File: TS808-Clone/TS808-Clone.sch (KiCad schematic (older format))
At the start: 44 parts, among them J1 AudioJack2, J2 Barrel_Jack, J3 AudioJack2, Q1 2N4401-AP, Q2 2N4401-AP, U1 RC4558

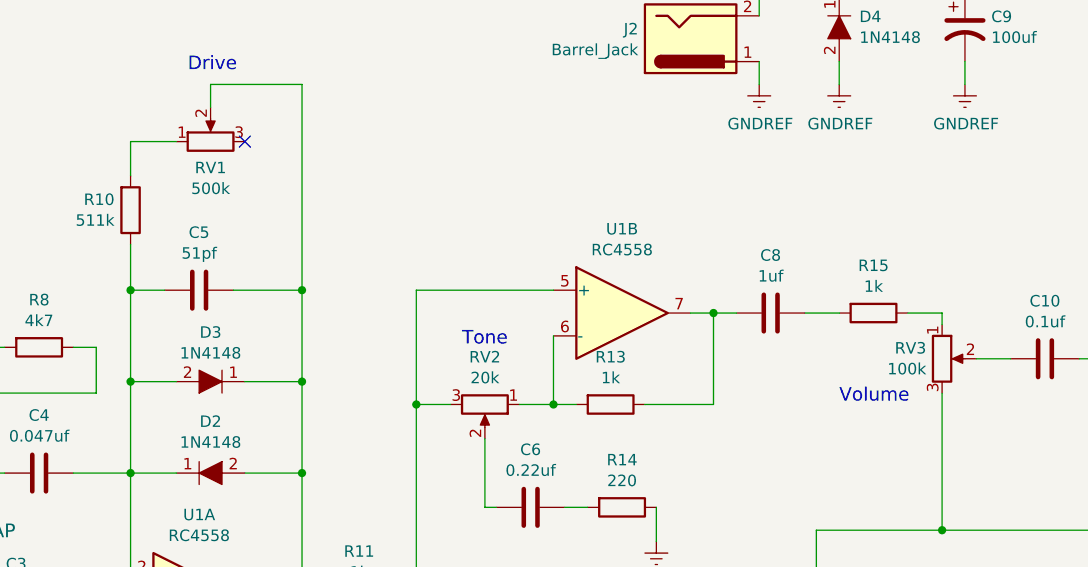
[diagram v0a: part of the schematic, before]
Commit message: Finished traces. Added fill with ground layer.
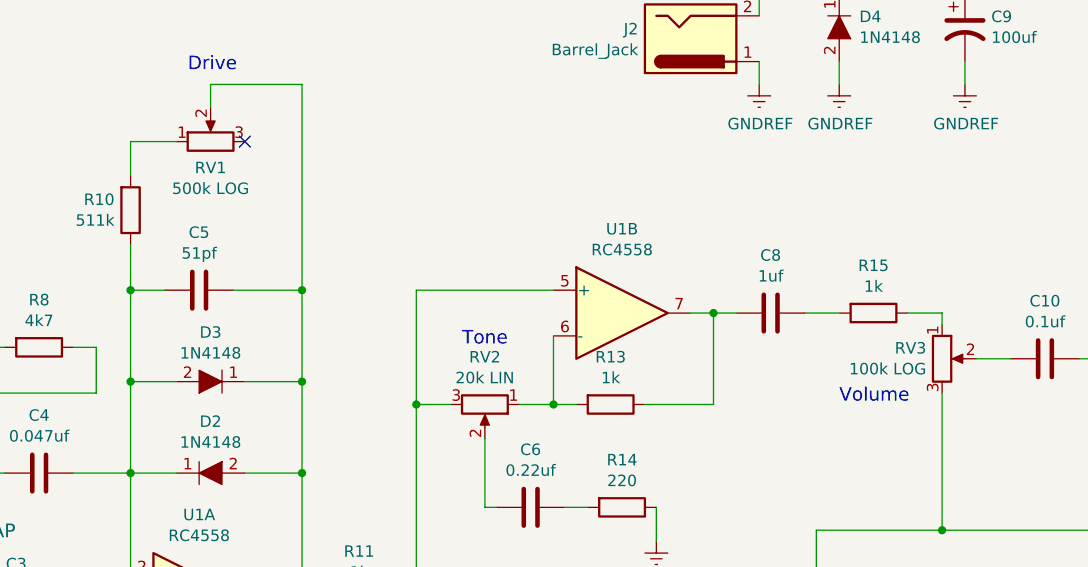
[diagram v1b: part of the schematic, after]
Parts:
- RV1: value 500k -> 500k LOG
- RV2: value 20k -> 20k LIN
- RV3: value 100k -> 100k LOG
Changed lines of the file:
@@
 P 5450 1900
 F 0 "RV1" V 5335 1900 50  0000 C CNN
-F 1 "500k" V 5244 1900 50  0000 C CNN
+F 1 "500k LOG" V 5244 1900 50  0000 C CNN
 F 2 "Potentiometer_THT:Potentiometer_TT_P0915N" H 5450 1900 50  0001 C CNN
 F 3 "https://www.ttelectronics.com/TTElectronics/media/ProductFiles/Potentiometers/Datasheets/P09x.pdf" H 5450 1900 50  0001 C CNN
@@
 P 6650 3050
 F 0 "RV2" V 6443 3050 50  0000 C CNN
-F 1 "20k" V 6534 3050 50  0000 C CNN
+F 1 "20k LIN" V 6534 3050 50  0000 C CNN
 F 2 "Potentiometer_THT:Potentiometer_TT_P0915N" H 6650 3050 50  0001 C CNN
 F 3 "https://www.ttelectronics.com/TTElectronics/media/ProductFiles/Potentiometers/Datasheets/P09x.pdf" H 6650 3050 50  0001 C CNN
@@
 P 8650 2850
 F 0 "RV3" H 8581 2896 50  0000 R CNN
-F 1 "100k" H 8581 2805 50  0000 R CNN
+F 1 "100k LOG" H 8581 2805 50  0000 R CNN
 F 2 "Potentiometer_THT:Potentiometer_TT_P0915N" H 8650 2850 50  0001 C CNN
 F 3 "https://www.ttelectronics.com/TTElectronics/media/ProductFiles/Potentiometers/Datasheets/P09x.pdf" H 8650 2850 50  0001 C CNN

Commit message: changed footprint for the pots
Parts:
- D2, D3, D4: symbol dk_Diodes-Rectifiers-Single:1N4148 -> TS808-Clone-rescue:1N4148-dk_Diodes-Rectifiers-Single
- Q1, Q2: symbol dk_Transistors-Bipolar-BJT-Single:2N4401-AP -> TS808-Clone-rescue:2N4401-AP-dk_Transistors-Bipolar-BJT-Single
- RV1, RV2, RV3: footprint Potentiometer_THT:Potentiometer_TT_P0915N -> Potentiometer_THT:Potentiometer_Bourns_PTV09A-1_Single_Vertical
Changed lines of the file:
@@
 $EndComp
 $Comp
-L dk_Diodes-Rectifiers-Single:1N4148 D4
+L TS808-Clone-rescue:1N4148-dk_Diodes-Rectifiers-Single D4
 U 1 1 5D46A900
 P 8200 1350
@@
 $EndComp
 $Comp
-L dk_Diodes-Rectifiers-Single:1N4148 D3
+L TS808-Clone-rescue:1N4148-dk_Diodes-Rectifiers-Single D3
 U 1 1 5D46D50E
 P 5500 2950
@@
 $EndComp
 $Comp
-L dk_Diodes-Rectifiers-Single:1N4148 D2
+L TS808-Clone-rescue:1N4148-dk_Diodes-Rectifiers-Single D2
 U 1 1 5D470632
 P 5400 3350
@@
 $EndComp
 $Comp
-L dk_Transistors-Bipolar-BJT-Single:2N4401-AP Q2
+L TS808-Clone-rescue:2N4401-AP-dk_Transistors-Bipolar-BJT-Single Q2
 U 1 1 5D472C75
 P 9900 2850
@@
 	2950 2500 2950 2650
 $Comp
-L dk_Transistors-Bipolar-BJT-Single:2N4401-AP Q1
+L TS808-Clone-rescue:2N4401-AP-dk_Transistors-Bipolar-BJT-Single Q1
 U 1 1 5D4A5B8B
 P 3950 3550
@@
 F 0 "RV1" V 5335 1900 50  0000 C CNN
 F 1 "500k LOG" V 5244 1900 50  0000 C CNN
-F 2 "Potentiometer_THT:Potentiometer_TT_P0915N" H 5450 1900 50  0001 C CNN
-F 3 "https://www.ttelectronics.com/TTElectronics/media/ProductFiles/Potentiometers/Datasheets/P09x.pdf" H 5450 1900 50  0001 C CNN
+F 2 "Potentiometer_THT:Potentiometer_Bourns_PTV09A-1_Single_Vertical" H 5450 1900 50  0001 C CNN
+F 3 "https://www.mouser.com/datasheet/2/54/ptv09-777818.pdf" H 5450 1900 50  0001 C CNN
 	1    5450 1900
 	0    -1   -1   0
@@
 F 0 "RV2" V 6443 3050 50  0000 C CNN
 F 1 "20k LIN" V 6534 3050 50  0000 C CNN
-F 2 "Potentiometer_THT:Potentiometer_TT_P0915N" H 6650 3050 50  0001 C CNN
-F 3 "https://www.ttelectronics.com/TTElectronics/media/ProductFiles/Potentiometers/Datasheets/P09x.pdf" H 6650 3050 50  0001 C CNN
+F 2 "Potentiometer_THT:Potentiometer_Bourns_PTV09A-1_Single_Vertical" H 6650 3050 50  0001 C CNN
+F 3 "https://www.mouser.com/datasheet/2/54/ptv09-777818.pdf" H 6650 3050 50  0001 C CNN
 	1    6650 3050
 	0    1    1    0
@@
 F 0 "RV3" H 8581 2896 50  0000 R CNN
 F 1 "100k LOG" H 8581 2805 50  0000 R CNN
-F 2 "Potentiometer_THT:Potentiometer_TT_P0915N" H 8650 2850 50  0001 C CNN
-F 3 "https://www.ttelectronics.com/TTElectronics/media/ProductFiles/Potentiometers/Datasheets/P09x.pdf" H 8650 2850 50  0001 C CNN
+F 2 "Potentiometer_THT:Potentiometer_Bourns_PTV09A-1_Single_Vertical" H 8650 2850 50  0001 C CNN
+F 3 "https://www.mouser.com/datasheet/2/54/ptv09-777818.pdf" H 8650 2850 50  0001 C CNN
 	1    8650 2850
 	1    0    0    -1

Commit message: moved jacks to final positions
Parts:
- D1: footprint LED_THT:LED_D5.0mm -> LED_SMD:LED_1206_3216Metric_Pad1.42x1.75mm_HandSolder
- RV1, RV2, RV3: footprint Potentiometer_THT:Potentiometer_Bourns_PTV09A-1_Single_Vertical -> TS808-Clone:Potentiometer_BournesProAudio_THT_vert
- S1: footprint TS808-Clone:Switch_3P3T_Footswitch_PC_THT -> TS808-Clone:Switch_3PDT_ESwitch_300_P1J1_VS2
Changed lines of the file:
@@
 F 0 "D1" H 3593 5316 50  0000 C CNN
 F 1 "LED" H 3593 5225 50  0000 C CNN
-F 2 "LED_THT:LED_D5.0mm" H 3600 5100 50  0001 C CNN
+F 2 "LED_SMD:LED_1206_3216Metric_Pad1.42x1.75mm_HandSolder" H 3600 5100 50  0001 C CNN
 F 3 "~" H 3600 5100 50  0001 C CNN
 	1    3600 5100
@@
 F 0 "RV1" V 5335 1900 50  0000 C CNN
 F 1 "500k LOG" V 5244 1900 50  0000 C CNN
-F 2 "Potentiometer_THT:Potentiometer_Bourns_PTV09A-1_Single_Vertical" H 5450 1900 50  0001 C CNN
+F 2 "TS808-Clone:Potentiometer_BournesProAudio_THT_vert" H 5450 1900 50  0001 C CNN
 F 3 "https://www.mouser.com/datasheet/2/54/ptv09-777818.pdf" H 5450 1900 50  0001 C CNN
 	1    5450 1900
@@
 F 0 "RV2" V 6443 3050 50  0000 C CNN
 F 1 "20k LIN" V 6534 3050 50  0000 C CNN
-F 2 "Potentiometer_THT:Potentiometer_Bourns_PTV09A-1_Single_Vertical" H 6650 3050 50  0001 C CNN
+F 2 "TS808-Clone:Potentiometer_BournesProAudio_THT_vert" H 6650 3050 50  0001 C CNN
 F 3 "https://www.mouser.com/datasheet/2/54/ptv09-777818.pdf" H 6650 3050 50  0001 C CNN
 	1    6650 3050
@@
 F 0 "RV3" H 8581 2896 50  0000 R CNN
 F 1 "100k LOG" H 8581 2805 50  0000 R CNN
-F 2 "Potentiometer_THT:Potentiometer_Bourns_PTV09A-1_Single_Vertical" H 8650 2850 50  0001 C CNN
+F 2 "TS808-Clone:Potentiometer_BournesProAudio_THT_vert" H 8650 2850 50  0001 C CNN
 F 3 "https://www.mouser.com/datasheet/2/54/ptv09-777818.pdf" H 8650 2850 50  0001 C CNN
 	1    8650 2850
@@
 F 0 "S1" H 9900 4535 50  0000 C CNN
 F 1 "Switch.3PDT.1" H 9900 4444 50  0000 C CNN
-F 2 "TS808-Clone:Switch_3P3T_Footswitch_PC_THT" H 9900 4250 50  0001 C CNN
-F 3 "https://cdn.shopify.com/s/files/1/1353/1185/files/4SFS3PDT-LS_PR_LSP_MSP_LSAU_Data_Sheet.pdf?12867592396497858423" H 9900 4250 50  0001 C CNN
+F 2 "TS808-Clone:Switch_3PDT_ESwitch_300_P1J1_VS2" H 9900 4250 50  0001 C CNN
+F 3 "https://www.mouser.com/datasheet/2/140/300-346108.pdf" H 9900 4250 50  0001 C CNN
 	3    9900 4250
 	-1   0    0    -1
@@
 F 0 "S1" H 4350 5485 50  0000 C CNN
 F 1 "Switch.3PDT.1" H 4350 5394 50  0000 C CNN
-F 2 "TS808-Clone:Switch_3P3T_Footswitch_PC_THT" H 4350 5200 50  0001 C CNN
-F 3 "https://cdn.shopify.com/s/files/1/1353/1185/files/4SFS3PDT-LS_PR_LSP_MSP_LSAU_Data_Sheet.pdf?12867592396497858423" H 4350 5200 50  0001 C CNN
+F 2 "TS808-Clone:Switch_3PDT_ESwitch_300_P1J1_VS2" H 4350 5200 50  0001 C CNN
+F 3 "https://www.mouser.com/datasheet/2/140/300-346108.pdf" H 4350 5200 50  0001 C CNN
 	2    4350 5200
 	-1   0    0    -1
@@
 F 0 "S1" H 2150 3685 50  0000 C CNN
 F 1 "Switch.3PDT.1" H 2150 3594 50  0000 C CNN
-F 2 "TS808-Clone:Switch_3P3T_Footswitch_PC_THT" H 2150 3400 50  0001 C CNN
-F 3 "https://cdn.shopify.com/s/files/1/1353/1185/files/4SFS3PDT-LS_PR_LSP_MSP_LSAU_Data_Sheet.pdf?12867592396497858423" H 2150 3400 50  0001 C CNN
+F 2 "TS808-Clone:Switch_3PDT_ESwitch_300_P1J1_VS2" H 2150 3400 50  0001 C CNN
+F 3 "https://www.mouser.com/datasheet/2/140/300-346108.pdf" H 2150 3400 50  0001 C CNN
 	1    2150 3400
 	-1   0    0    -1
